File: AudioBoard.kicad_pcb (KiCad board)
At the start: 2 copper layers, 100 x 100 mm, 72 parts, among them IC1 AMS1117-5.0, IC2 PCM5102APWR, IC3 PCM1803ADBR, J1 I2S2_OPT, J10 POT, J11 POT, J12 POT, J13 57PC5F, J14 57PC5F, J15 RCA_2x2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

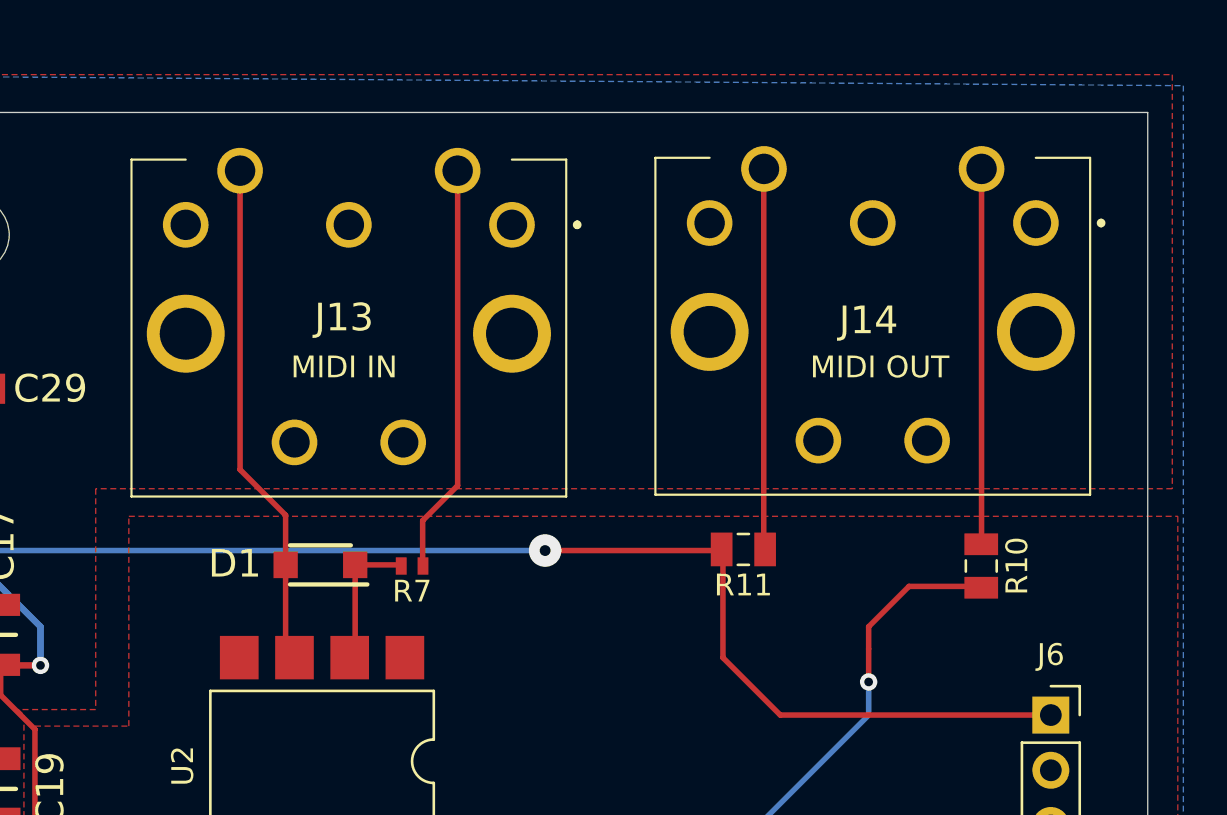
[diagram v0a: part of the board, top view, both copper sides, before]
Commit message: Updated MIDI schematic and orientation and to do list. Note: Gerber not updated.
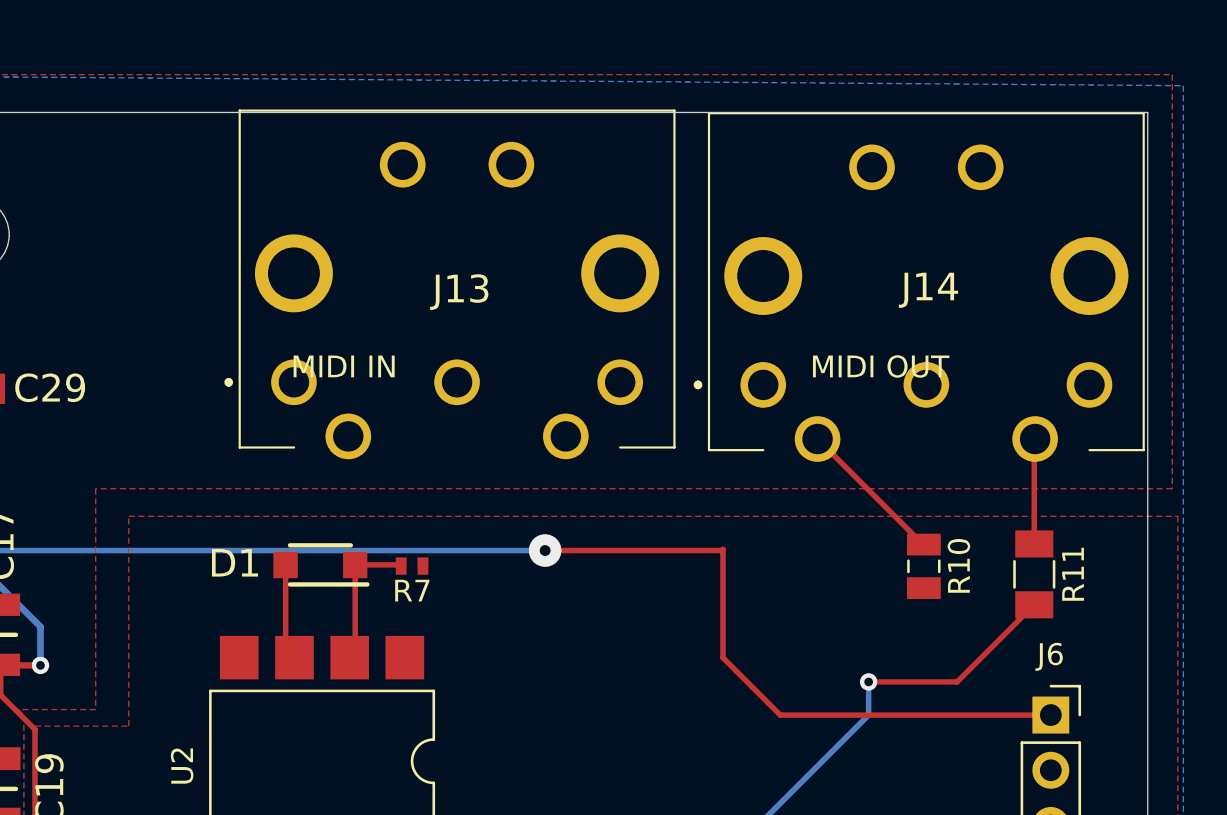
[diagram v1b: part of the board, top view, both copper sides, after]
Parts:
- R10: value 47 -> 33
- R11: value 47 -> 10; footprint SamacSys_Parts:R_0805_JLCPCB -> SamacSys_Parts:R_1206_JLCPCB
- moved J14 14.6 mm to (132.3, 62.5), turned to 270 degrees
- moved R11 13.4 mm to (144.8, 71.2), turned to 270 degrees
- moved J13 12.4 mm to (110.7, 62.4), turned to 270 degrees
- moved R10 2.64 mm to (139.7, 70.9)
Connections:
- R10 pad 2: /MIDI_OUT -> +3V3
- R11 pad 2: +5V -> /MIDI_OUT
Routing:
- net Net-(D1-Pad2): track 23.4 -> 4.44 mm
- net Net-(J13-Pad4): track 18.9 -> 0.00 mm
- net Net-(J14-Pad5): track 17.5 -> 4.84 mm
- net Net-(J14-Pad4): track 17.3 -> 6.90 mm
- net /MIDI_OUT: track 137.4 -> 138.0 mm

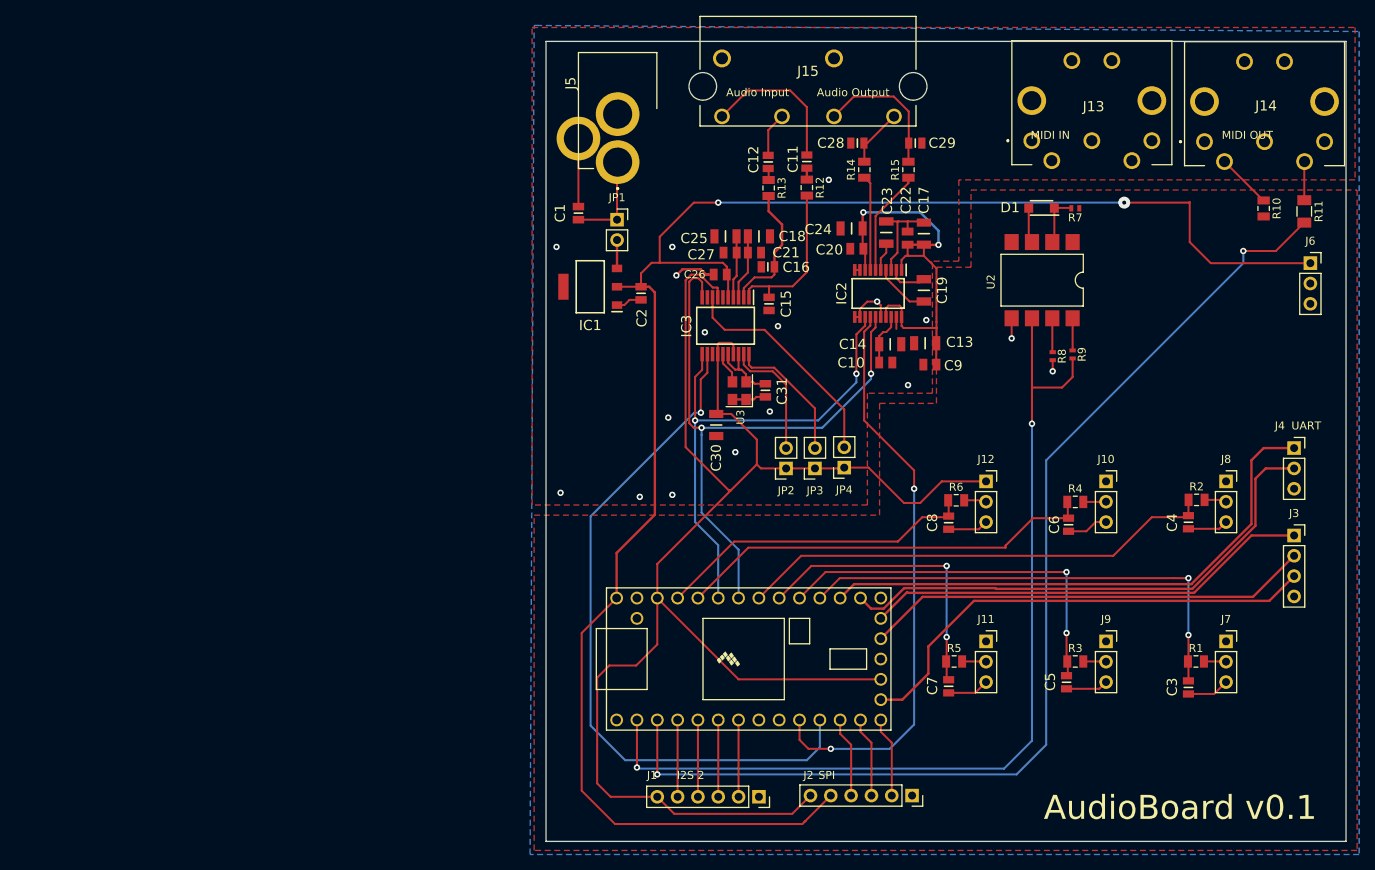
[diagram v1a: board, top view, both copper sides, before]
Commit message: Aligned outputs, started on tracing and connected Pi Innovo header in schematic.
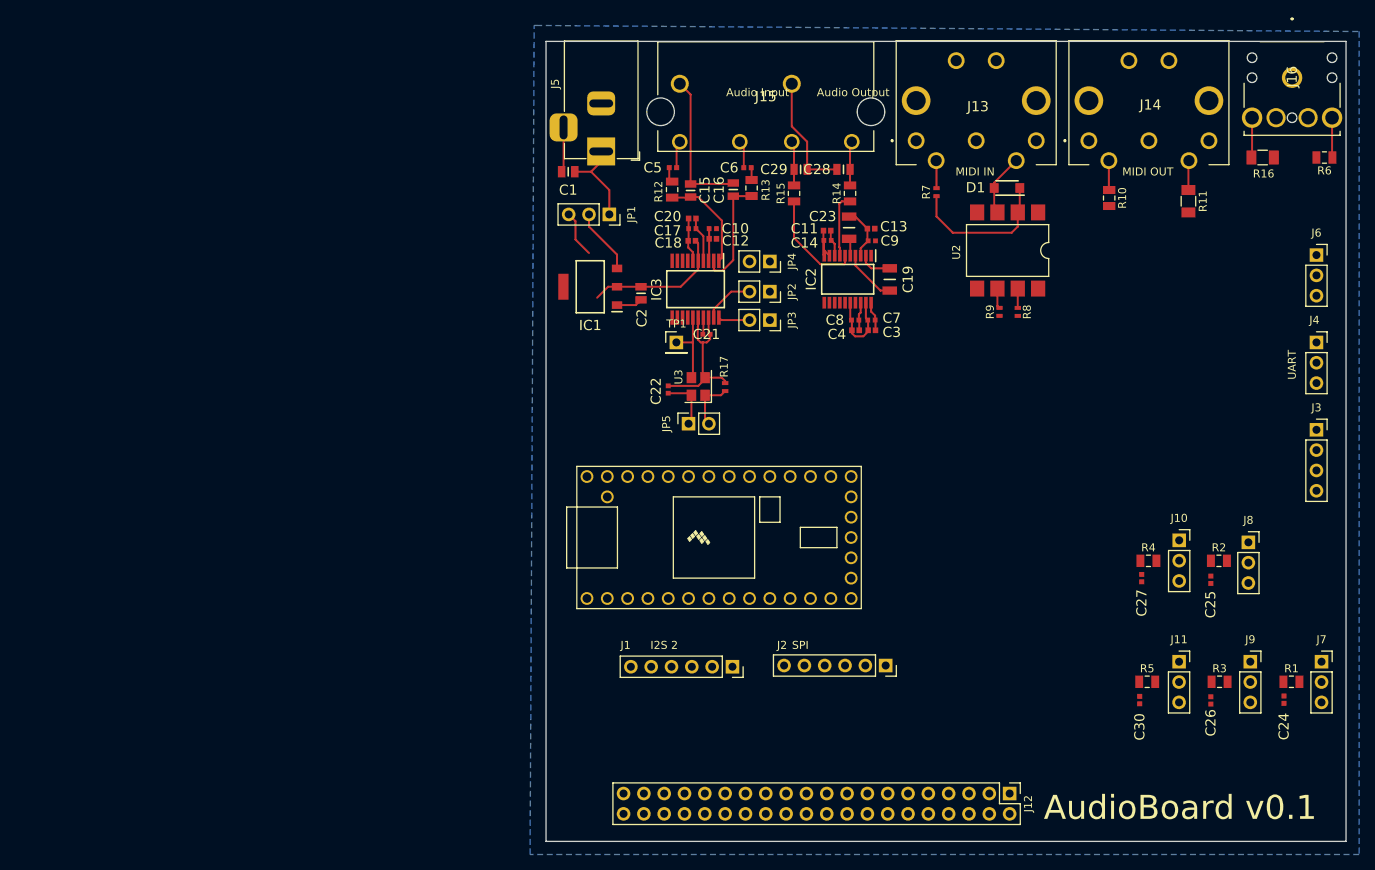
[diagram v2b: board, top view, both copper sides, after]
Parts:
- removed C31: 10nF50V, SamacSys_Parts:CAPC2012X65N
- added J16: SJ1-3523N, SamacSys_Parts:SJ13523N, F.Cu at (143.3, 50.0)
- added JP5: OSC_DIS, Connector_PinSocket_2.54mm:PinSocket_1x02_P2.54mm_Vertical, F.Cu at (67.8, 97.8)
- added R16: 10, SamacSys_Parts:R_1206_JLCPCB, F.Cu at (139.6, 64.5)
- added R17: 10k, SamacSys_Parts:R_0402_JLCPCB, F.Cu at (72.4, 93.2)
- added TP1: TestPoint, Connector_PinHeader_2.54mm:PinHeader_1x01_P2.54mm_Vertical, F.Cu at (66.3, 87.6)
- C10, C21, C22, C9: value 10uF25V -> 100nF16V; footprint SamacSys_Parts:CAPC2012X145N -> SamacSys_Parts:CAPC1005X55N
- C11, C12, C3, C4: value 1uF50V -> 10uF6.3V; footprint SamacSys_Parts:CAPC2012X135N -> SamacSys_Parts:CAPC1005X70N
- C13, C18: value 100nF50V -> 10uF6.3V; footprint SamacSys_Parts:CAPC3216X100N -> SamacSys_Parts:CAPC1005X70N
- C14, C17: value 100nF50V -> 100nF16V; footprint SamacSys_Parts:CAPC3216X100N -> SamacSys_Parts:CAPC1005X55N
- C20: value 10uF25V -> 10uF6.3V; footprint SamacSys_Parts:CAPC2012X145N -> SamacSys_Parts:CAPC1005X70N
- C24, C25, C30: value 100nF50V -> 1uF25V; footprint SamacSys_Parts:CAPC3216X100N -> SamacSys_Parts:CAPC1005X60N
- C26, C27: value 10uF25V -> 1uF25V; footprint SamacSys_Parts:CAPC2012X145N -> SamacSys_Parts:CAPC1005X60N
- C5, C6: value 1uF50V -> 1uF25V; footprint SamacSys_Parts:CAPC2012X135N -> SamacSys_Parts:CAPC1005X60N
- C7, C8: value 1uF50V -> 100nF16V; footprint SamacSys_Parts:CAPC2012X135N -> SamacSys_Parts:CAPC1005X55N
- J12: value POT -> Raspberry_Pi_2_3; footprint Connector_PinSocket_2.54mm:PinSocket_1x03_P2.54mm_Vertical -> Connector_PinHeader_2.54mm:PinHeader_2x20_P2.54mm_Vertical
- J5: footprint SamacSys_Parts:163179PHEX -> SamacSys_Parts:BarrelJack_Horizontal
- JP1: value POWER_SWITCH -> Teensy supply select; footprint Connector_PinSocket_2.54mm:PinSocket_1x02_P2.54mm_Vertical -> Connector_PinSocket_2.54mm:PinSocket_1x03_P2.54mm_Vertical
- R6: value 470 -> 33
- moved C26 81.2 mm to (133.1, 132.4), turned to 270 degrees
- moved C5 81.0 mm to (65.9, 65.8), turned to 180 degrees
- moved C24 79.9 mm to (142.2, 132.3), turned to 270 degrees
- moved C25 74.3 mm to (133.1, 117.3), turned to 270 degrees
- moved C27 65.6 mm to (124.5, 117.1), turned to 270 degrees
- moved C30 63.1 mm to (124.2, 132.3)
- moved R6 62.9 mm to (147.3, 64.5), turned to 180 degrees
- moved C6 60.0 mm to (75.2, 65.8), turned to 0 degrees
- moved C3 59.7 mm to (90.7, 86.1), turned to 0 degrees
- moved C4 48.0 mm to (88.7, 86.1), turned to 180 degrees
- moved C7 46.8 mm to (90.7, 84.8), turned to 180 degrees
- moved J12 39.1 mm to (108.0, 144.0), turned to 270 degrees
- moved C22 35.4 mm to (65.3, 93.5)
- moved C17 29.0 mm to (68.3, 73.4), turned to 180 degrees
- moved C8 27.9 mm to (88.6, 84.8), turned to 0 degrees
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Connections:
- C10 pad 1: GND -> Net-(C10-Pad1)
- C10 pad 2: Net-(C10-Pad2) -> GND
- C11 pad 1: /Audio IO (I2S)/RCA_IN_L -> GND
- C11 pad 2: Net-(C11-Pad2) -> +3V3
- C12 pad 1: /Audio IO (I2S)/RCA_IN_R -> GND
- C12 pad 2: Net-(C12-Pad2) -> Net-(C10-Pad1)
- C13 pad 1: +3V3 -> GND
- C13 pad 2: GND -> +3V3
- C14 pad 1: GND -> +3V3
- C14 pad 2: Net-(C10-Pad2) -> GND
- C17 pad 1: +3V3 -> Net-(C17-Pad1)
- C18 pad 2: Net-(C18-Pad2) -> +5V
- C20 pad 1: +3V3 -> GND
- C20 pad 2: GND -> Net-(C17-Pad1)
- C21 pad 1: GND -> +3V3
- C21 pad 2: Net-(C18-Pad2) -> GND
- C24 pad 1: +3V3 -> /POT1
- C25 pad 1: GND -> /POT4
- C25 pad 2: Net-(C25-Pad2) -> GND
- C26 pad 1: GND -> /POT2
- C26 pad 2: +5V -> GND
- C27 pad 1: GND -> /POT5
- C27 pad 2: Net-(C25-Pad2) -> GND
- C3 pad 1: /POT1 -> GND
- C3 pad 2: GND -> +3V3
- C30 pad 1: +3V3 -> /POT3
- C4 pad 1: /POT4 -> Net-(C4-Pad1)
- C5 pad 1: /POT2 -> /Audio IO (I2S)/RCA_IN_L
- C5 pad 2: GND -> Net-(C5-Pad2)
- C6 pad 1: /POT5 -> /Audio IO (I2S)/RCA_IN_R
- C6 pad 2: GND -> Net-(C6-Pad2)
- C7 pad 1: /POT3 -> +3V3
- C8 pad 1: /POT6 -> GND
- C8 pad 2: GND -> Net-(C4-Pad1)
- IC1 pad 4: Net-(IC1-Pad4) -> (no net)
- IC2 pad 18: Net-(C10-Pad2) -> Net-(C4-Pad1)
- IC3 pad 3: Net-(C18-Pad2) -> Net-(C10-Pad1)
- IC3 pad 4: Net-(C25-Pad2) -> Net-(C17-Pad1)
- J12 pad 2: Net-(J12-Pad2) -> +5V
- J12 pad 3: GND -> (no net)
- J13 pad 1: Net-(J13-Pad1) -> (no net)
- J13 pad 2: Net-(J13-Pad2) -> (no net)
- J13 pad 3: Net-(J13-Pad3) -> (no net)
- J13 pad MH1: Net-(J13-PadMH1) -> (no net)
- J13 pad MH2: Net-(J13-PadMH2) -> (no net)
- J14 pad 1: Net-(J14-Pad1) -> (no net)
- J14 pad 3: Net-(J14-Pad3) -> (no net)
- J14 pad MH1: Net-(J14-PadMH1) -> (no net)
- J14 pad MH2: Net-(J14-PadMH2) -> (no net)
- R12 pad 1: Net-(C11-Pad2) -> Net-(C5-Pad2)
- R13 pad 1: Net-(C12-Pad2) -> Net-(C6-Pad2)
- R6 pad 1: /POT6 -> Net-(J16-Pad3)
- R6 pad 2: Net-(J12-Pad2) -> +3V3
- U1 pad 10: /I2S_DOUT -> /I2S_DIN
- U1 pad 11: /I2S_DIN -> (no net)
- U1 pad 20: Net-(U1-Pad20) -> (no net)
- U1 pad 24: /POT2 -> /MIDI_OUT2
- U1 pad 25: /POT3 -> /POT2
- U1 pad 26: /POT4 -> /POT3
- U1 pad 29: /POT5 -> /POT4
- U1 pad 30: /POT6 -> /POT5
- U1 pad 34: Net-(U1-Pad34) -> /V_USB
- U1 pad 8: Net-(U1-Pad8) -> (no net)
- U1 pad 9: Net-(U1-Pad9) -> /I2S_DOUT
- U2 pad 1: Net-(U2-Pad1) -> (no net)
- U2 pad 4: Net-(U2-Pad4) -> (no net)
- U3 pad 1: Net-(C31-Pad2) -> Net-(JP5-Pad2)
- U3 pad 4: Net-(C31-Pad2) -> +3V3
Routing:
- net +3V3: track 258.7 -> 15.8 mm, vias 2 -> 0
- net +5V: track 215.2 -> 17.8 mm, vias 2 -> 0
- net /MIDI_OUT: track 138.0 -> 0.00 mm, vias 2 -> 0
- net /MIDI_IN: track 117.6 -> 2.51 mm, vias 2 -> 0
- net /I2S_DIN: track 87.5 -> 0.00 mm, vias 1 -> 0
- net /I2S_LRCK: track 78.3 -> 0.00 mm, vias 2 -> 0
- net /I2S_DOUT: track 72.4 -> 0.00 mm, vias 2 -> 0
- net /UART_OPT_RX: track 69.2 -> 0.00 mm
- net /UART_OPT_TX: track 65.5 -> 0.00 mm
- net /I2S_BCK: track 62.8 -> 0.00 mm, vias 2 -> 0
- net Net-(J3-Pad3): track 60.0 -> 0.00 mm
- net /POT4: track 60.0 -> 0.00 mm
- net /POT1: track 59.9 -> 0.00 mm, vias 2 -> 0
- net Net-(J3-Pad1): track 56.0 -> 0.00 mm
- net Net-(J3-Pad2): track 56.0 -> 0.00 mm
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- removed copper zone on F.Cu, net +3V3
- removed copper zone on F.Cu, net GND

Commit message: Updated PCB traces.
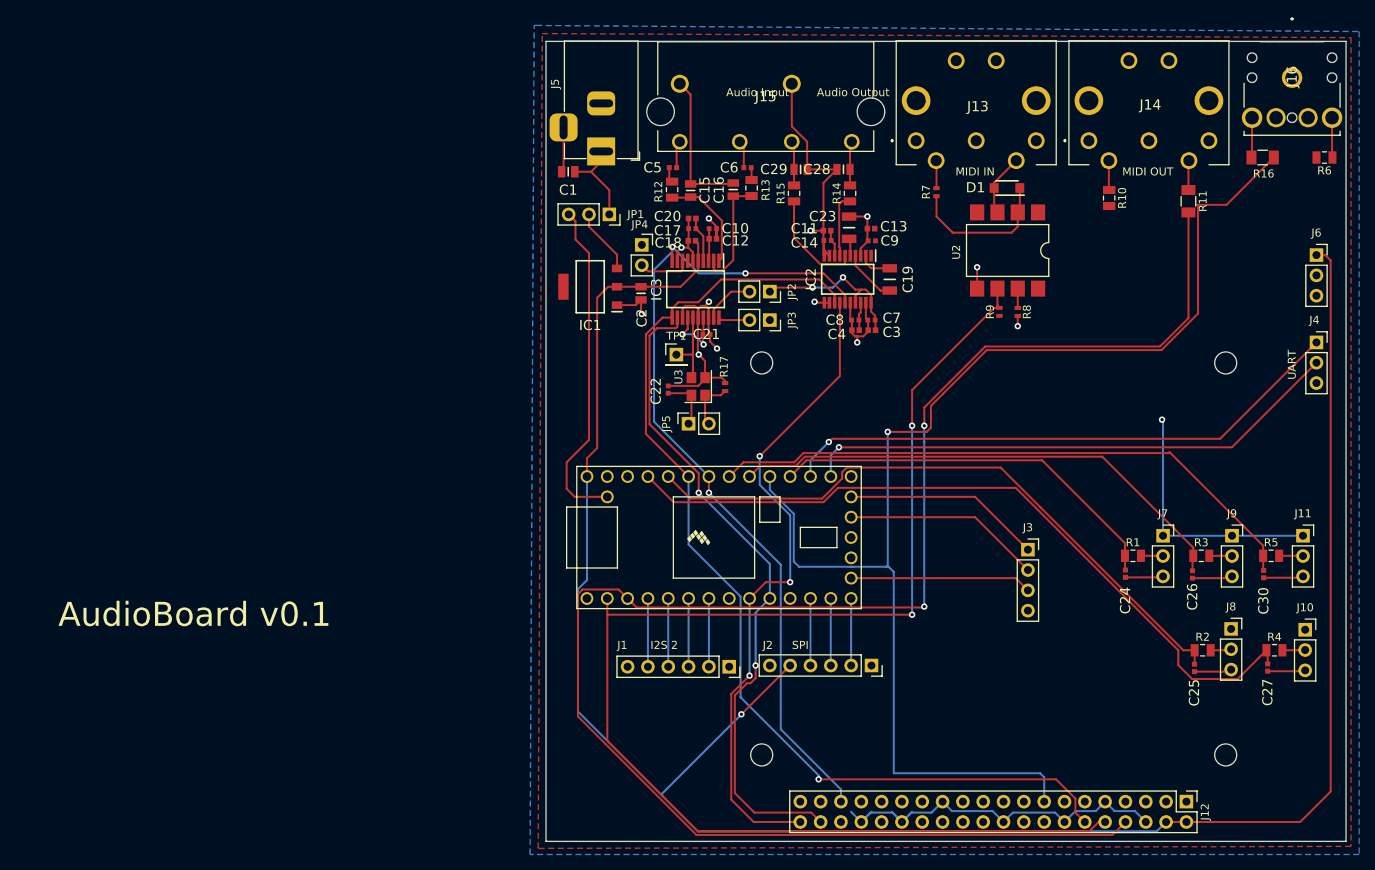
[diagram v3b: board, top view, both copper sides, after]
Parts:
- added REF**: Raspberry_Pi_3B+_MountingHoles, SamacSys_Parts:Raspberry_Pi_3B+_MountingHoles, F.Cu at (80.6, 136.7)
- moved J3 39.1 mm to (110.2, 113.5)
- moved C24 25.3 mm to (122.4, 116.5)
- moved R1 25.3 mm to (123.4, 114.3)
- moved J7 25.3 mm to (127.1, 111.8)
- moved J12 22.1 mm to (130.0, 145.0)
- moved J11 22.1 mm to (144.6, 111.8)
- moved C30 22.1 mm to (139.7, 116.6)
- moved R5 22.1 mm to (140.6, 114.3)
- moved C27 19.3 mm to (140.2, 128.3)
- moved J10 19.3 mm to (144.9, 123.5)
- moved R4 19.3 mm to (141.0, 126.1)
- moved JP4 16.1 mm to (62.0, 75.4), turned to 0 degrees
- moved C26 15.9 mm to (130.8, 116.6)
- moved J9 15.9 mm to (135.7, 111.8)
- moved R3 15.9 mm to (131.9, 114.3)
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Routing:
- net +5V: track 17.8 -> 264.2 mm, vias 0 -> 1
- net /MIDI_OUT: track 0.00 -> 210.8 mm, vias 0 -> 2
- net /MIDI_IN: track 2.51 -> 169.1 mm, vias 0 -> 2
- net /MIDI_OUT2: track 0.00 -> 161.5 mm, vias 0 -> 1
- net /I2S_BCK: track 0.00 -> 130.0 mm, vias 0 -> 1
- net GND: track 90.3 -> 198.3 mm, vias 0 -> 12
- net /I2S_LRCK: track 0.00 -> 106.8 mm, vias 0 -> 3
- net /POT5: track 0.00 -> 93.6 mm
- net /I2S_DIN: track 0.00 -> 82.8 mm, vias 0 -> 2
- net /I2S_DOUT: track 0.00 -> 82.5 mm, vias 0 -> 3
- net /POT4: track 0.00 -> 80.4 mm
- net /POT3: track 0.00 -> 76.0 mm
- net /UART_OPT_RX: track 0.00 -> 71.4 mm, vias 0 -> 1
- net /UART_OPT_TX: track 0.00 -> 68.1 mm, vias 0 -> 1
- net /POT2: track 0.00 -> 64.1 mm
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- added copper zone on F.Cu, net +3V3
